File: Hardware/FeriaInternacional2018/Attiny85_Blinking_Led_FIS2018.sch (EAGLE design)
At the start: 9 parts, among them U1 ATTINY85-20P

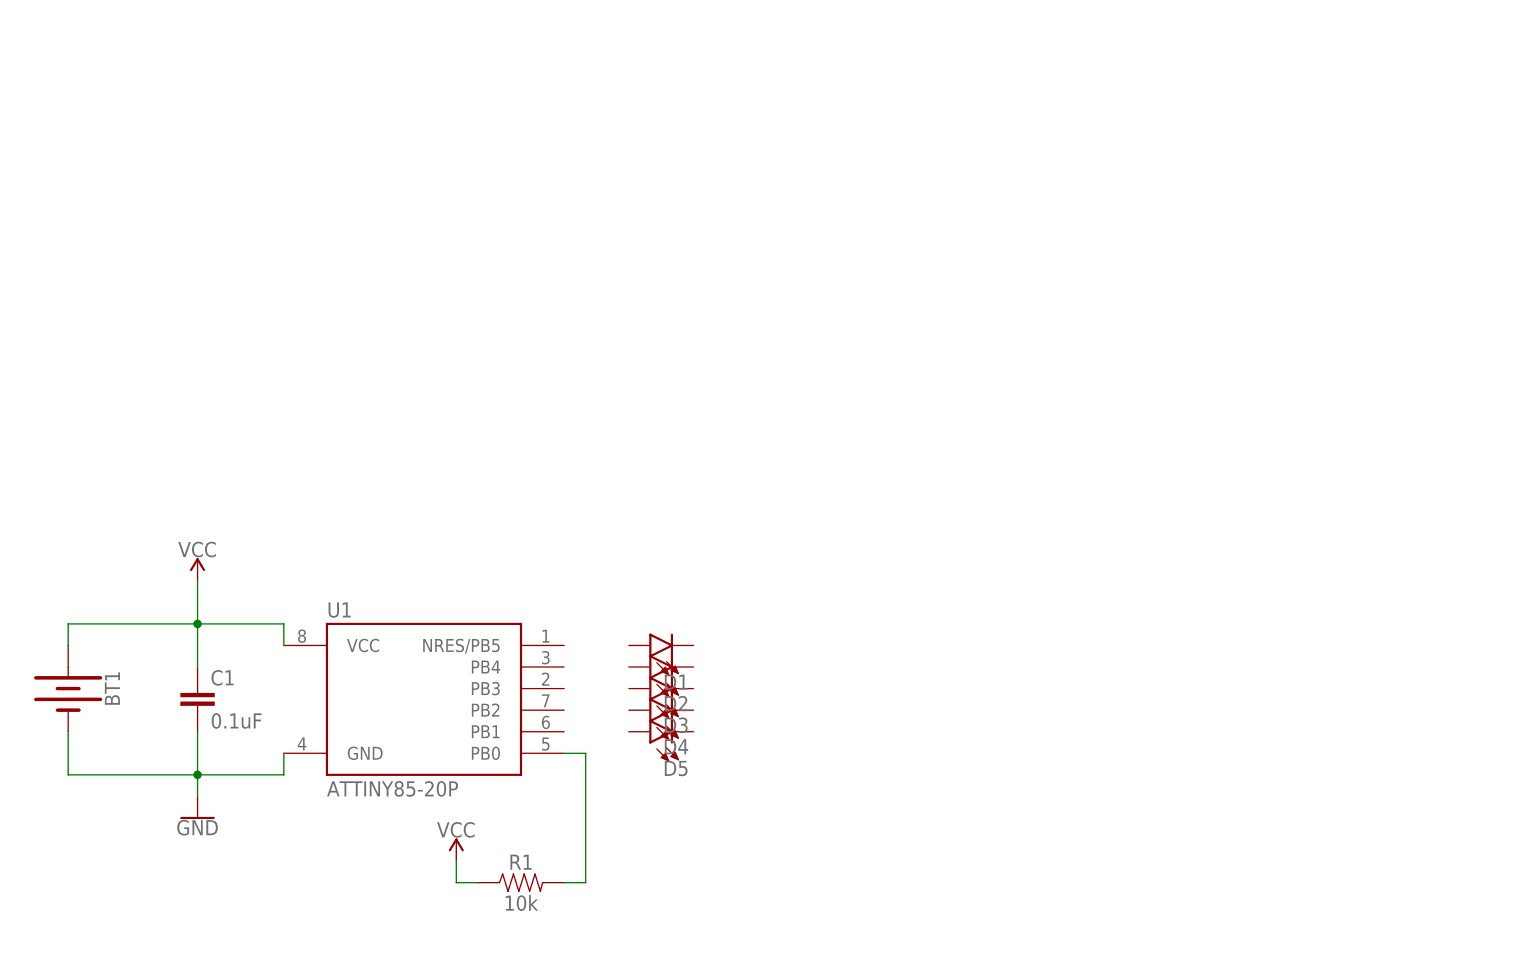
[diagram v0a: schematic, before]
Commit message: I did a charlieplexing with attiny85, i use 20 leds, i make a board, but inst ready, just i did a file
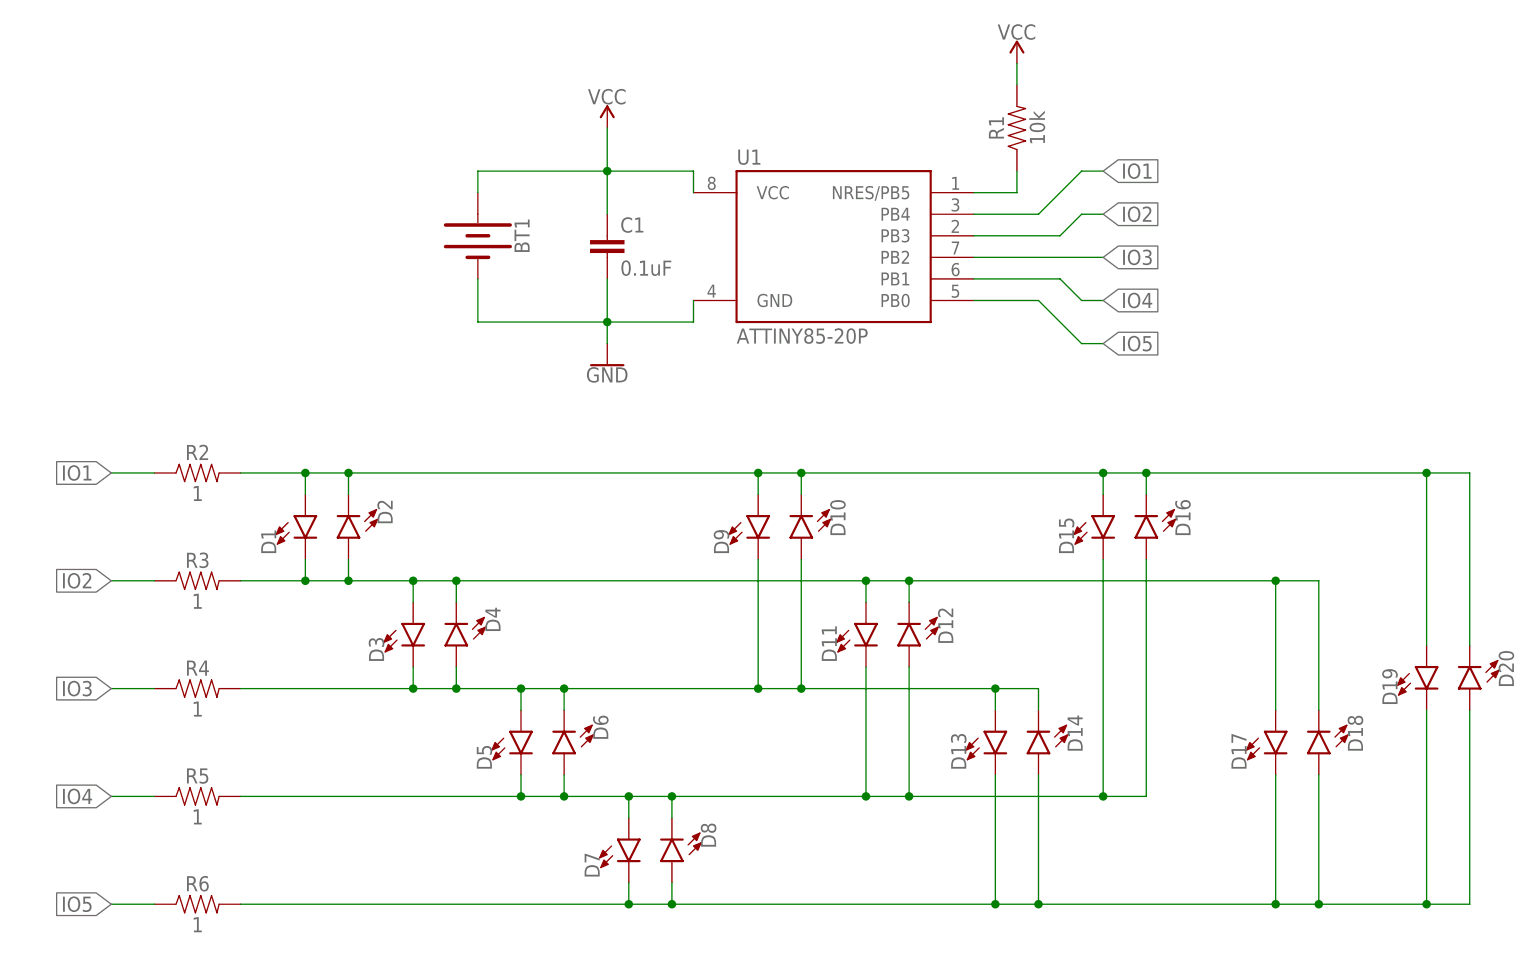
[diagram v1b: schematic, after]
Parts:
- added D10, D11, D12, D13, D14, D15, D16, D17, D18, D19, D20, D6, D7, D8, D9: (no value), SparkFun-LED:LED3MM
- added R2, R3, R4, R5, R6: 1, SparkFun-Resistors:1OHM-0603-1/10W-1%
- D1, D2, D3, D4, D5: device SparkFun-LED:LED-3MM-NO_SILK -> SparkFun-LED:LED3MM
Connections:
- new net IO1: D1.A, D10.C, D15.A, D16.C, D19.A, D2.C, D20.C, D9.A, R2.1, R2.2, U1.PB4
- new net IO2: D1.C, D11.A, D12.C, D17.A, D18.C, D2.A, D3.A, D4.C, R3.1, R3.2, U1.PB3
- new net IO3: D10.A, D13.A, D14.C, D3.C, D4.A, D5.A, D6.C, D9.C, R4.1, R4.2, U1.PB2
- new net IO4: D11.C, D12.A, D15.C, D16.A, D5.C, D6.A, D7.A, D8.C, R5.1, R5.2, U1.PB1
- new net IO5: D13.C, D14.A, D17.C, D18.A, D19.C, D20.A, D7.C, D8.A, R6.1, R6.2, U1.PB0
- net N$1: now also R1.1, U1.NRES/PB5; no longer R1.2, U1.PB0
- net VCC: now also R1.2; no longer R1.1
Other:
- moved on the sheet: BT1, C1, D1, D2, D3, D4, D5, R1, U1

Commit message: Add a SPST switch, order and design a PCB circuit, doenst route yet
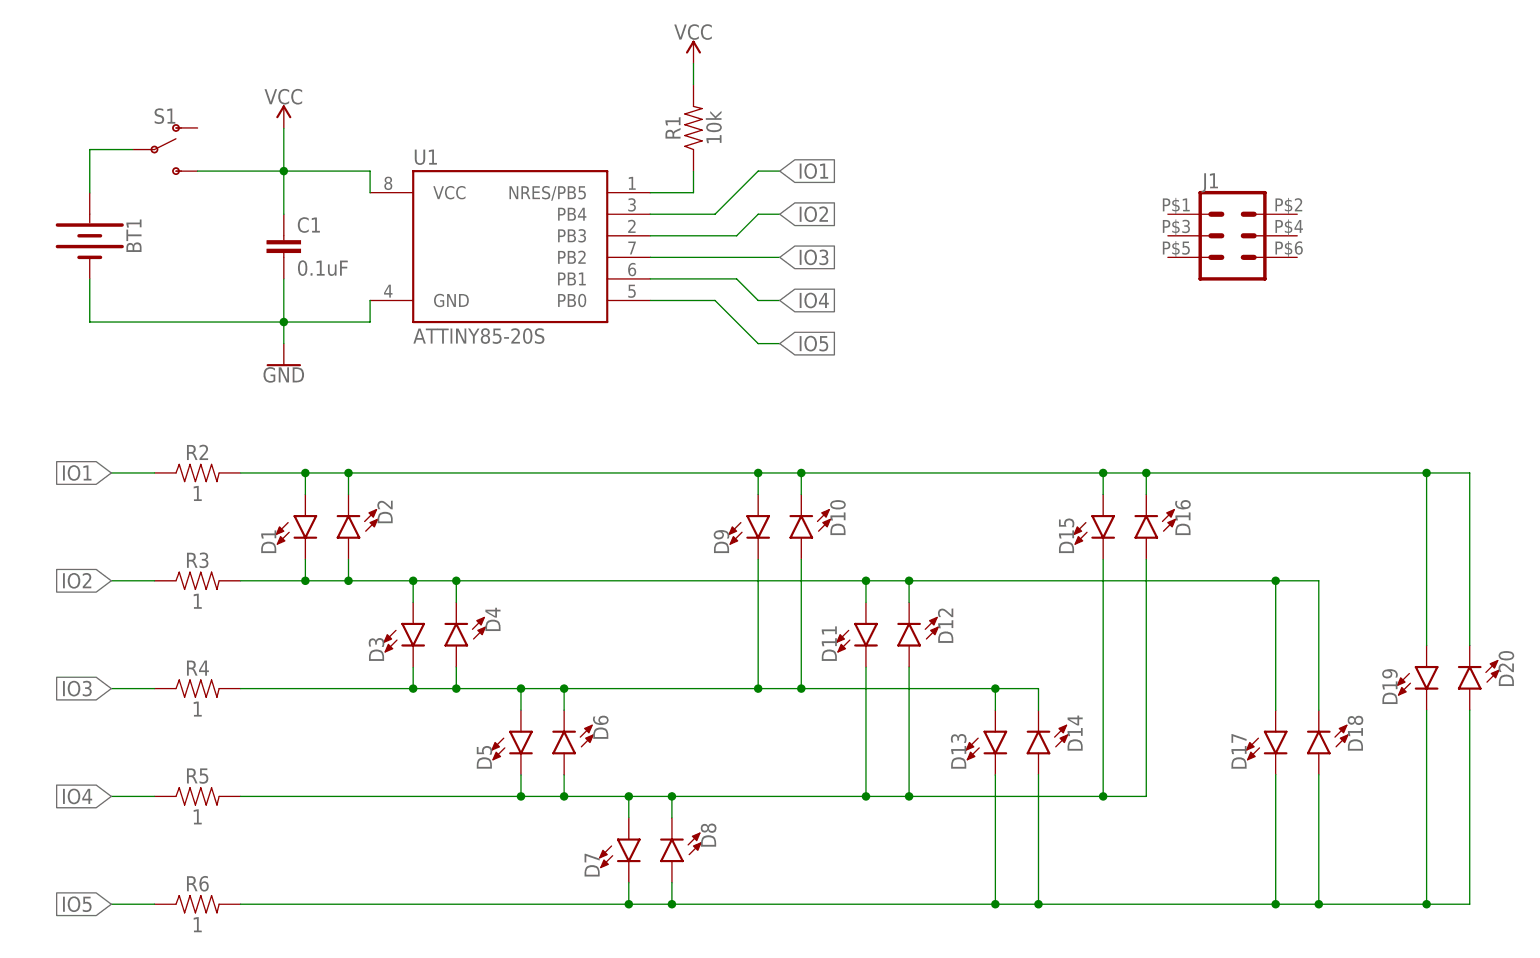
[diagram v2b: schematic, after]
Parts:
- added J1: (no value), SparkFun-Connectors:CONN_03X2POGO_PINS
- added S1: (no value), SparkFun-Switches:SWITCH-SPDT-SMD-RIGHT-ANGLE
- BT1: device SparkFun-Batteries:BATTERY-12MM_SMD -> SparkFun-Batteries:BATTERY-20MM_SMD_4LEGS
- U1: value ATTINY85-20P -> ATTINY85-20S; device _hhn_attiny25_45_85:ATTINY85-20P -> _hhn_attiny25_45_85:ATTINY85-20S
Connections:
- new net N$2: BT1.+, S1.P
- net VCC: now also S1.S; no longer BT1.+
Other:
- moved on the sheet: BT1, C1, R1, U1

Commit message: Disenño de placa, posicion de componentes y ruteo de lineas
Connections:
- net IO1 renamed IO11
- net IO2 renamed IO22
- net IO3 renamed IO33
- net IO4 renamed IO44
- net IO5 renamed IO55

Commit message: add port spi, has a desing art, add holes for badge and pin
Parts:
- R1: device SparkFun-Resistors:10KOHM-0603-1/10W-1% -> SparkFun-Resistors:10KOHM-HORIZ-1/4W-1%
- R2, R3, R4, R5, R6: value 1 -> 10k; device SparkFun-Resistors:1OHM-0603-1/10W-1% -> SparkFun-Resistors:10KOHM-HORIZ-1/4W-1%
- U1: value ATTINY85-20S -> ATTINY85-20P; device _hhn_attiny25_45_85:ATTINY85-20S -> _hhn_attiny25_45_85:ATTINY85-20P
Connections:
- new net IO1: J1.2, R2.2, U1.PB4
- new net IO2: R3.2, U1.PB3
- new net IO3: J1.4, R4.2, U1.PB2
- new net IO4: J1.6, R5.2, U1.PB1
- new net IO5: J1.3, R6.2, U1.PB0
- net GND: now also J1.1
- net IO11: no longer R2.2, U1.PB4
- net IO22: no longer R3.2, U1.PB3
- net IO33: no longer R4.2, U1.PB2
- net IO44: no longer R5.2, U1.PB1
- net IO55: no longer R6.2, U1.PB0
- net VCC: now also J1.5
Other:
- moved on the sheet: R2, R3, R4, R5, R6

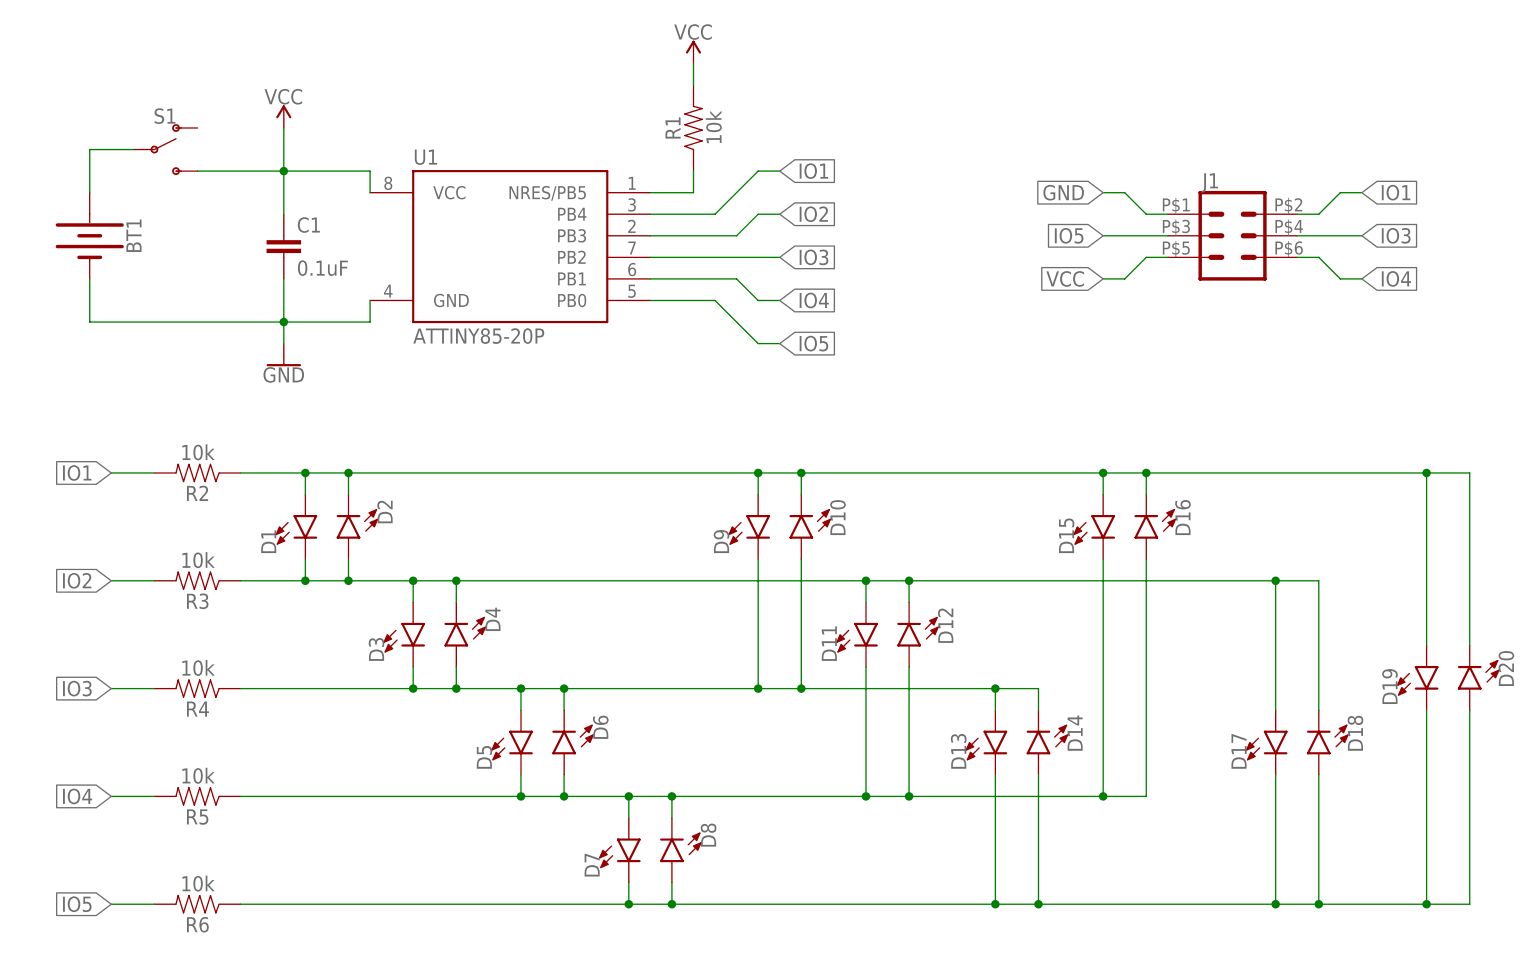
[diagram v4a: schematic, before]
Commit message: add logo ALSW, reorder route, redimension pcb
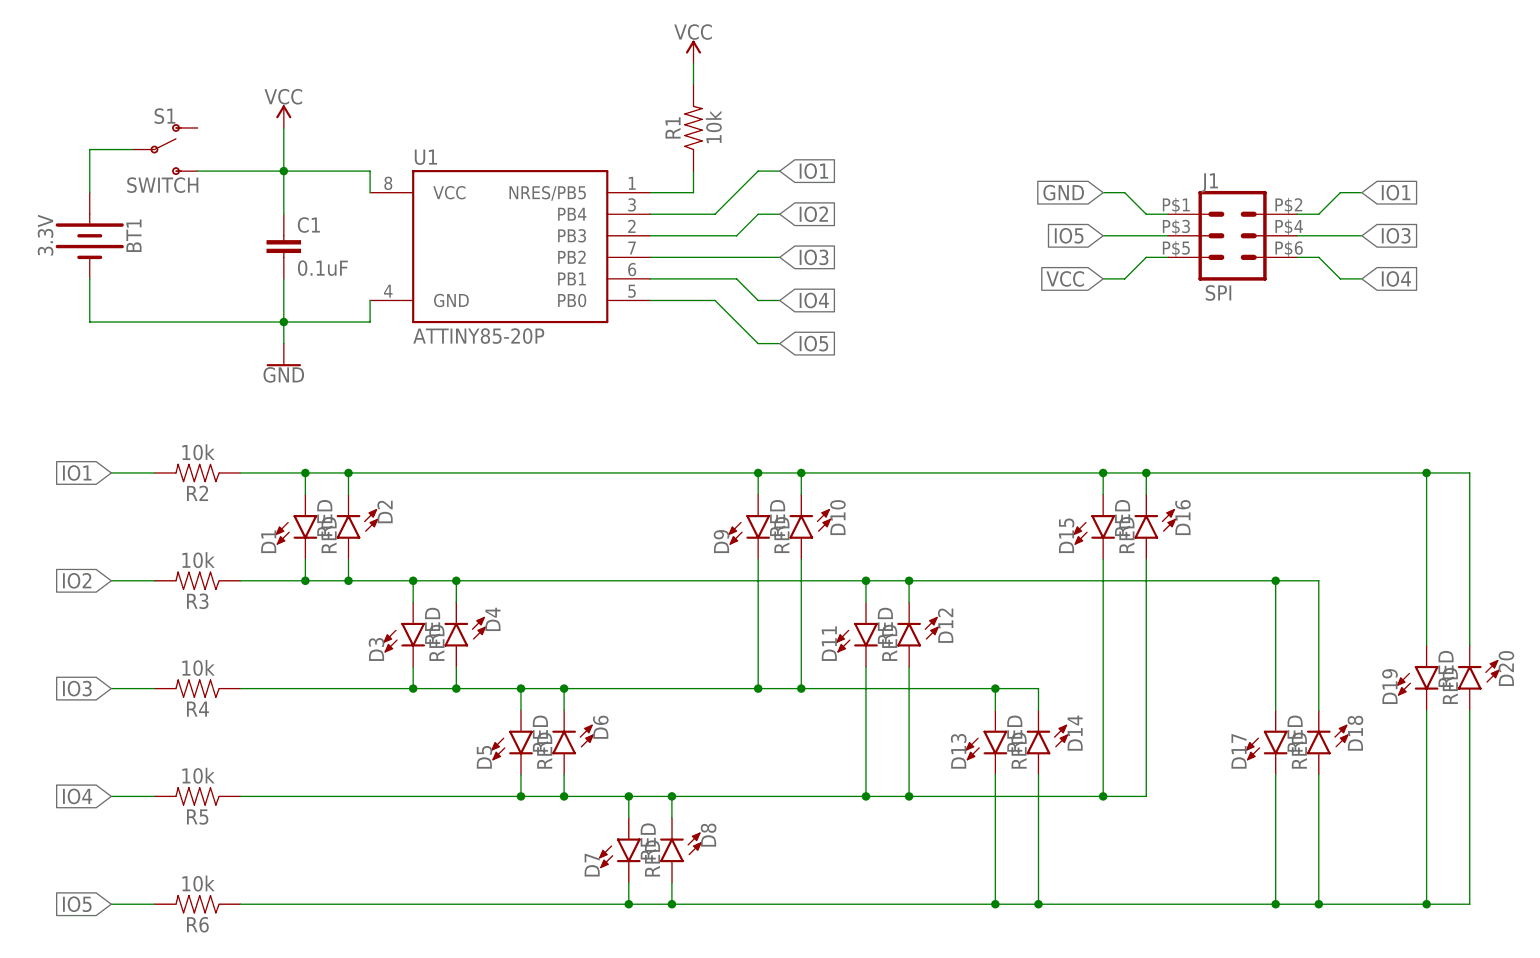
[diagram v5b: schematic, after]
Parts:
- BT1: value (none) -> 3.3V
- D1, D10, D11, D12, D13, D14, D15, D16, D17, D18, D19, D2, D20, D3, D4, D5, D6, D7, D8, D9: value (none) -> RED
- J1: value (none) -> SPI
- S1: value (none) -> SWITCH
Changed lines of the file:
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@@
 <parts>
 <part name="U1" library="_hhn_attiny25_45_85" deviceset="ATTINY85*" device="P" technology="-20" value="ATTINY85-20P"/>
-<part name="BT1" library="SparkFun-Batteries" deviceset="BATTERY" device="-20MM_SMD_4LEGS"/>
+<part name="BT1" library="SparkFun-Batteries" deviceset="BATTERY" device="-20MM_SMD_4LEGS" value="3.3V"/>
 <part name="C1" library="SparkFun-Capacitors" deviceset="0.1UF" device="-0603-25V-(+80/-20%)" value="0.1uF"/>
 <part name="R1" library="SparkFun-Resistors" deviceset="10KOHM" device="-HORIZ-1/4W-1%" value="10k"/>
@@
 <part name="GND1" library="SparkFun-PowerSymbols" deviceset="GND" device=""/>
 <part name="SUPPLY2" library="SparkFun-PowerSymbols" deviceset="VCC" device=""/>
-<part name="D1" library="SparkFun-LED" deviceset="LED" device="3MM"/>
-<part name="D2" library="SparkFun-LED" deviceset="LED" device="3MM"/>
-<part name="D3" library="SparkFun-LED" deviceset="LED" device="3MM"/>
-<part name="D4" library="SparkFun-LED" deviceset="LED" device="3MM"/>
-<part name="D5" library="SparkFun-LED" deviceset="LED" device="3MM"/>
-<part name="D6" library="SparkFun-LED" deviceset="LED" device="3MM"/>
-<part name="D7" library="SparkFun-LED" deviceset="LED" device="3MM"/>
-<part name="D8" library="SparkFun-LED" deviceset="LED" device="3MM"/>
-<part name="D9" library="SparkFun-LED" deviceset="LED" device="3MM"/>
-<part name="D10" library="SparkFun-LED" deviceset="LED" device="3MM"/>
-<part name="D11" library="SparkFun-LED" deviceset="LED" device="3MM"/>
-<part name="D12" library="SparkFun-LED" deviceset="LED" device="3MM"/>
-<part name="D13" library="SparkFun-LED" deviceset="LED" device="3MM"/>
-<part name="D14" library="SparkFun-LED" deviceset="LED" device="3MM"/>
-<part name="D15" library="SparkFun-LED" deviceset="LED" device="3MM"/>
-<part name="D16" library="SparkFun-LED" deviceset="LED" device="3MM"/>
-<part name="D17" library="SparkFun-LED" deviceset="LED" device="3MM"/>
-<part name="D18" library="SparkFun-LED" deviceset="LED" device="3MM"/>
-<part name="D19" library="SparkFun-LED" deviceset="LED" device="3MM"/>
-<part name="D20" library="SparkFun-LED" deviceset="LED" device="3MM"/>
+<part name="D1" library="SparkFun-LED" deviceset="LED" device="3MM" value="RED"/>
+<part name="D2" library="SparkFun-LED" deviceset="LED" device="3MM" value="RED"/>
+<part name="D3" library="SparkFun-LED" deviceset="LED" device="3MM" value="RED"/>
+<part name="D4" library="SparkFun-LED" deviceset="LED" device="3MM" value="RED"/>
+<part name="D5" library="SparkFun-LED" deviceset="LED" device="3MM" value="RED"/>
+<part name="D6" library="SparkFun-LED" deviceset="LED" device="3MM" value="RED"/>
+<part name="D7" library="SparkFun-LED" deviceset="LED" device="3MM" value="RED"/>
+<part name="D8" library="SparkFun-LED" deviceset="LED" device="3MM" value="RED"/>
+<part name="D9" library="SparkFun-LED" deviceset="LED" device="3MM" value="RED"/>
+<part name="D10" library="SparkFun-LED" deviceset="LED" device="3MM" value="RED"/>
+<part name="D11" library="SparkFun-LED" deviceset="LED" device="3MM" value="RED"/>
+<part name="D12" library="SparkFun-LED" deviceset="LED" device="3MM" value="RED"/>
+<part name="D13" library="SparkFun-LED" deviceset="LED" device="3MM" value="RED"/>
+<part name="D14" library="SparkFun-LED" deviceset="LED" device="3MM" value="RED"/>
+<part name="D15" library="SparkFun-LED" deviceset="LED" device="3MM" value="RED"/>
+<part name="D16" library="SparkFun-LED" deviceset="LED" device="3MM" value="RED"/>
+<part name="D17" library="SparkFun-LED" deviceset="LED" device="3MM" value="RED"/>
+<part name="D18" library="SparkFun-LED" deviceset="LED" device="3MM" value="RED"/>
+<part name="D19" library="SparkFun-LED" deviceset="LED" device="3MM" value="RED"/>
+<part name="D20" library="SparkFun-LED" deviceset="LED" device="3MM" value="RED"/>
 <part name="R2" library="SparkFun-Resistors" deviceset="10KOHM" device="-HORIZ-1/4W-1%" value="10k"/>
 <part name="R3" library="SparkFun-Resistors" deviceset="10KOHM" device="-HORIZ-1/4W-1%" value="10k"/>
@@
 <part name="R5" library="SparkFun-Resistors" deviceset="10KOHM" device="-HORIZ-1/4W-1%" value="10k"/>
 <part name="R6" library="SparkFun-Resistors" deviceset="10KOHM" device="-HORIZ-1/4W-1%" value="10k"/>
-<part name="S1" library="SparkFun-Switches" deviceset="SWITCH-SPDT" device="-SMD-RIGHT-ANGLE"/>
-<part name="J1" library="SparkFun-Connectors" deviceset="CONN_03X2" device="POGO_PINS"/>
+<part name="S1" library="SparkFun-Switches" deviceset="SWITCH-SPDT" device="-SMD-RIGHT-ANGLE" value="SWITCH"/>
+<part name="J1" library="SparkFun-Connectors" deviceset="CONN_03X2" device="POGO_PINS" value="SPI"/>
 <part name="FRAME1" library="SparkFun-Aesthetics" deviceset="FRAME-A4L" device=""/>
 </parts>
@@
 </sheet>
 </sheets>
+<errors>
+</errors>
 </schematic>
 </drawing>
